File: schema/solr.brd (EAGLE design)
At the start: 33 x 43.2 mm, 17 parts, among them J1 ISP, U1 ATMEGA328P, U2 HMC5883L

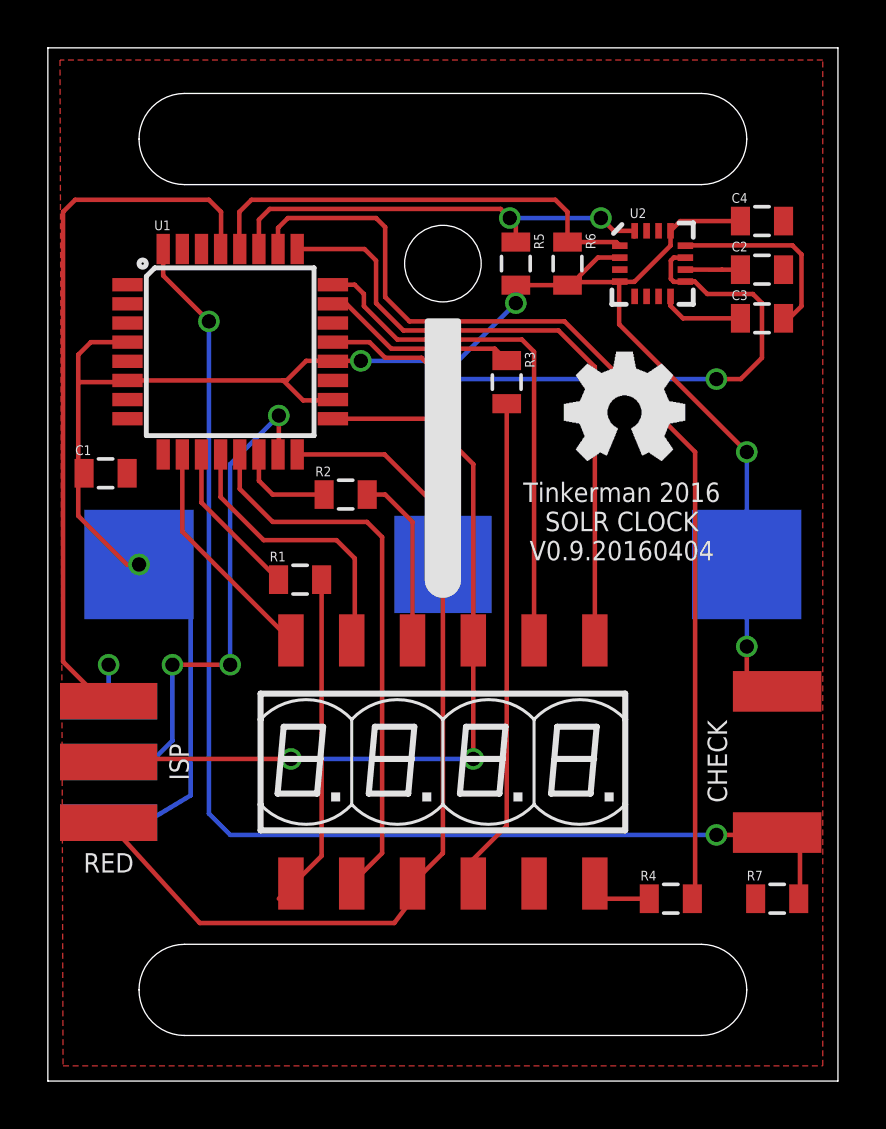
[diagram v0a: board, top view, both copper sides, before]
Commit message: First version of the PCB sent to fab
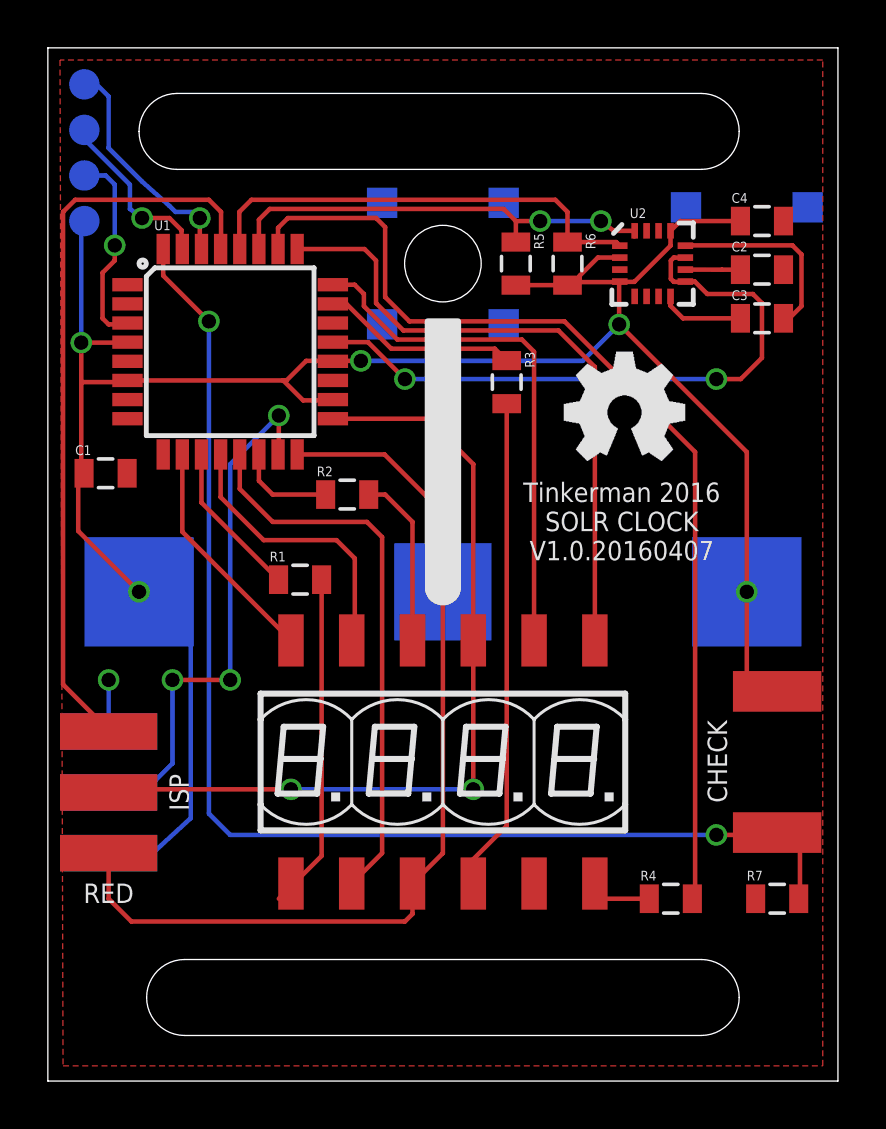
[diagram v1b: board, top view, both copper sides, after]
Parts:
- added JP1: (no value), xose:1X04_SMD_ROUND_PADS
- added U$1: M3_WELDING_NUTFLAT, xose:M3_WELDING_NUT_FLAT
- added U$2: M3_WELDING_NUTSTAND, xose:M3_WELDING_NUT_STAND
- moved J1 1.27 mm to (2.54, 12.1)
- moved BATT 1.14 mm to (16.5, 20.4)
- moved R2 0.06 mm to (12.5, 24.5)
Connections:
- new net RX: JP1.P$4, U1.30
- new net TX: JP1.P$3, U1.31
- net GND: now also JP1.P$2
- net VCC: now also JP1.P$1
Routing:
- net VCC: track 83.9 -> 94.9 mm
- net GND: track 36.2 -> 46.3 mm, vias 3 -> 4
- net RX: track 0.00 -> 9.70 mm, vias 0 -> 1
- net TX: track 0.00 -> 7.35 mm, vias 0 -> 1
- net SCK: track 34.3 -> 35.9 mm
- net RST: track 30.0 -> 31.2 mm
- net MOSI: track 21.5 -> 22.6 mm
- net MISO: track 38.8 -> 39.5 mm
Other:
- outline, holes or cut-outs redrawn
- board text added: "GND"
- board text added: "RX"
- board text added: "TX"
- board text added: "Tinkerman 2016 SOLR CLOCK V1.0.20160407"
- board text added: "VCC"
- board text removed: "Tinkerman 2016 SOLR CLOCK V0.9.20160404"
